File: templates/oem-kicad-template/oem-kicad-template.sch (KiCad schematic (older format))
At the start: 0 parts

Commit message: added icon to template, added atmega to template schematic
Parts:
- added IC?: ATMEGA16M1, Housings_QFP:TQFP-32_7x7mm_Pitch0.8mm, symbol ATMEGA16M1
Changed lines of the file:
@@
 LIBS:contrib
 LIBS:valves
+LIBS:formula
 EELAYER 25 0
 EELAYER END
@@
 Comment4 ""
 $EndDescr
+$Comp
+L ATMEGA16M1 IC?
+U 1 1 59E01442
+P 4950 4300
+F 0 "IC?" H 4000 6130 50  0000 L BNN
+F 1 "ATMEGA16M1" H 5450 2900 50  0000 L BNN
+F 2 "Housings_QFP:TQFP-32_7x7mm_Pitch0.8mm" H 4950 4300 50  0000 C CIN
+F 3 "" H 4950 4300 50  0000 C CNN
+	1    4950 4300
+	1    0    0    -1
+$EndComp
 $EndSCHEMATC

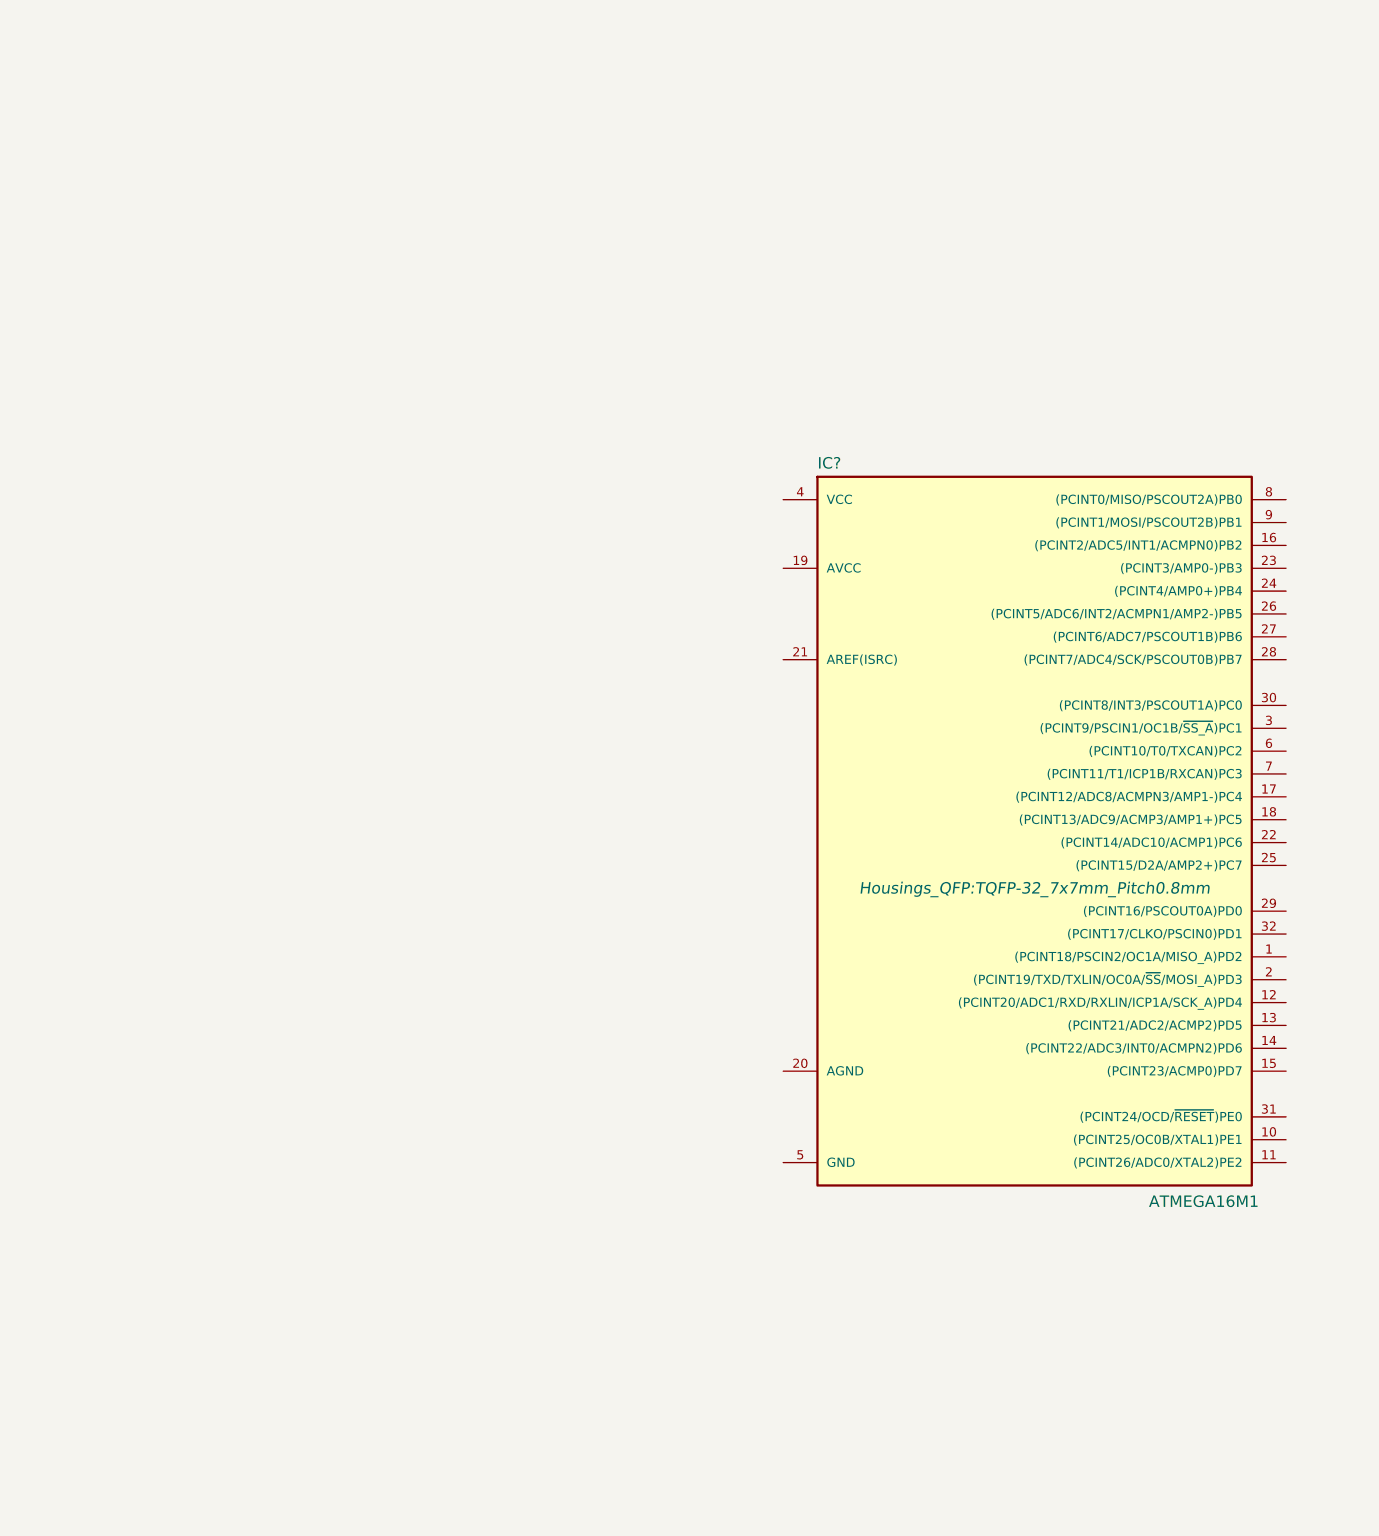
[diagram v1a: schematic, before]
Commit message: added buck to template, working on adding atmega
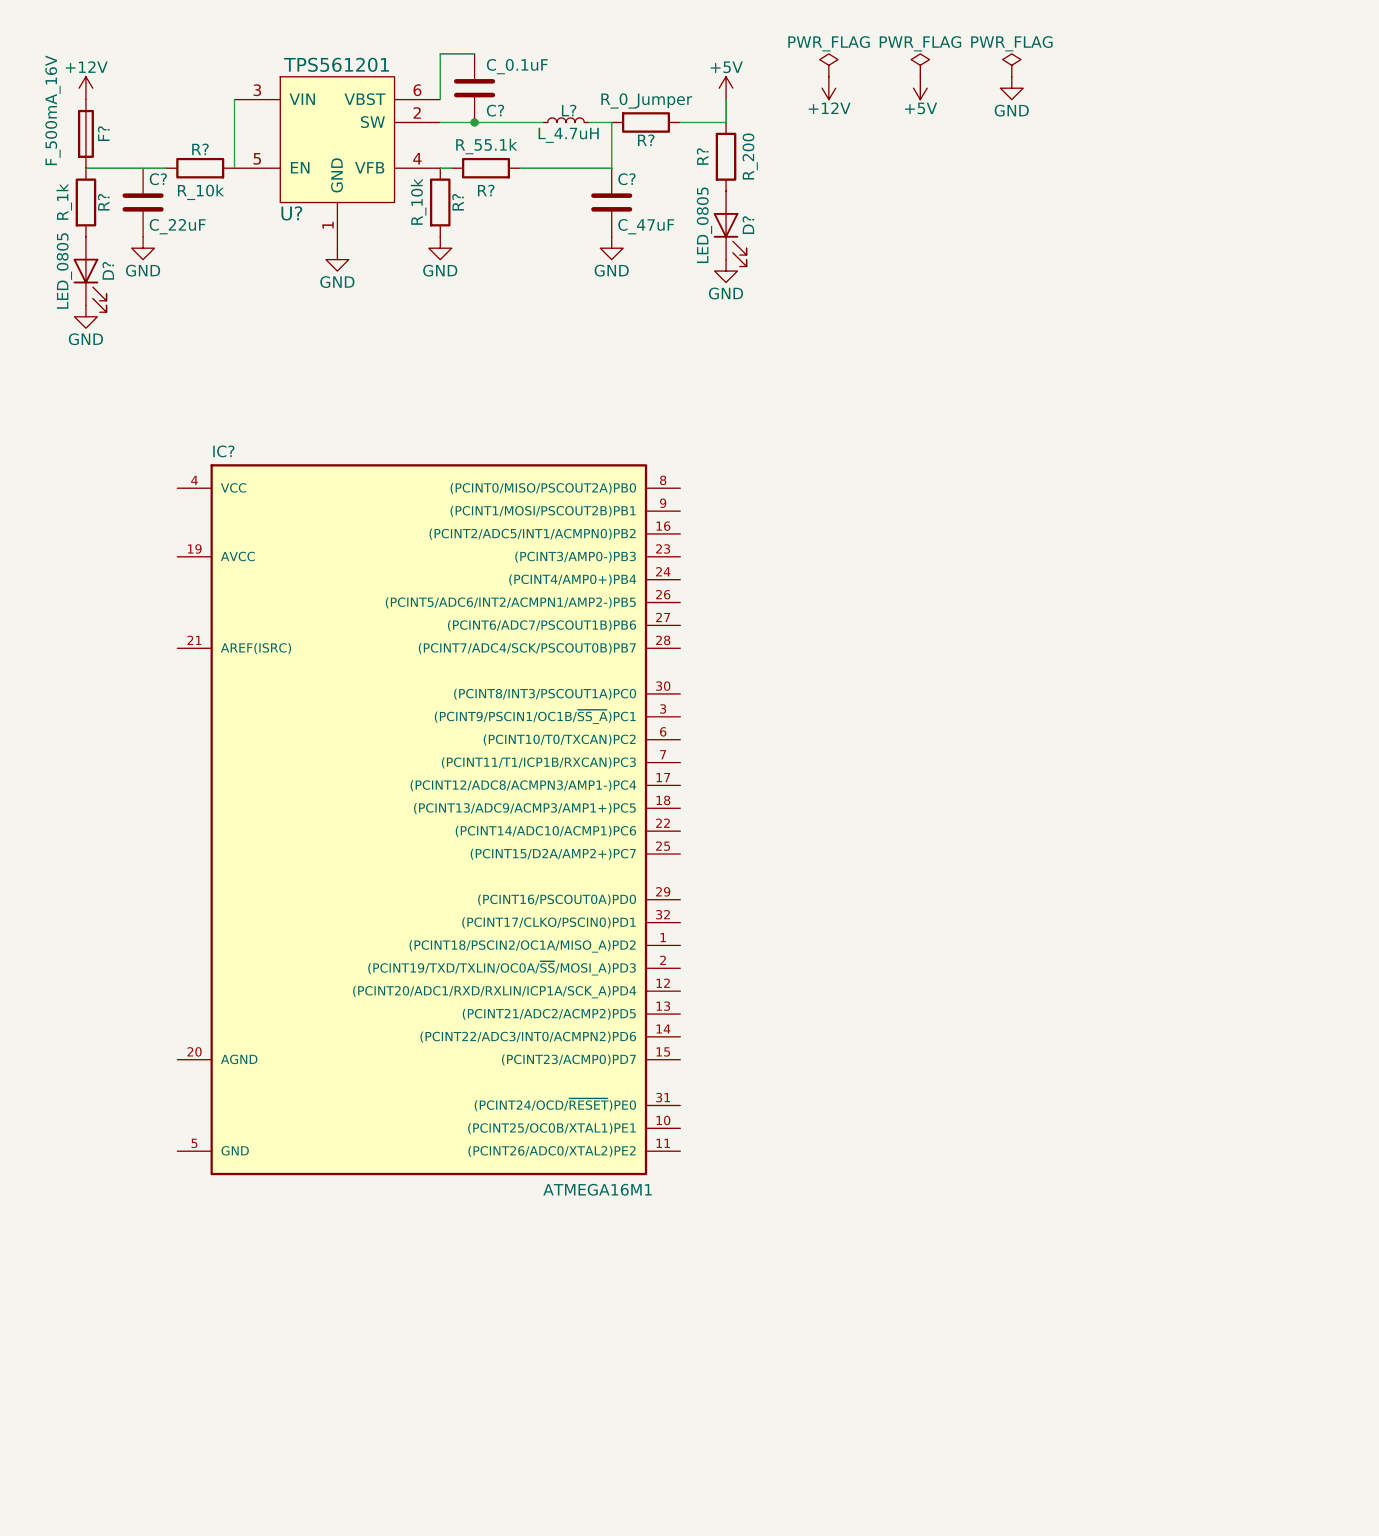
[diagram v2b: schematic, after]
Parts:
- removed IC?: ATMEGA16M1, Housings_QFP:TQFP-32_7x7mm_Pitch0.8mm, symbol ATMEGA16M1
- added C?: C_0.1uF, Capacitors_SMD:C_0805, symbol C_0.1uF
- added C?: C_22uF, Capacitors_SMD:C_1206, symbol C_22uF
- added C?: C_47uF, Capacitors_SMD:C_0805, symbol C_47uF
- added D? (x2): LED_0805, LEDs:LED_0805, symbol LED_0805
- added F?: F_500mA_16V, footprints:Fuse_1210, symbol F_500mA_16V
- added IC?: ATMEGA16M1, Housings_QFP:TQFP-32_7x7mm_Pitch0.8mm, symbol ATMEGA16M1
- added L?: L_4.7uH, footprints:4.7uH_Inductor_OEM, symbol L_4.7uH
- added R? (x2): R_10k, Resistors_SMD:R_0805, symbol R_10k
- added R?: R_1k, Resistors_SMD:R_0805, symbol R_1k
- added R?: R_55.1k, Resistors_SMD:R_0805, symbol R_55.1k
- added R?: R_200, Resistors_SMD:R_0805, symbol R_200
- added R?: R_0_Jumper, Resistors_SMD:R_2512, symbol R_0_Jumper
- added U?: TPS561201, TO_SOT_Packages_SMD:SOT-23-6, symbol TPS561201
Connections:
- new net: F?.2, R?.1, R?.1
- new net: R?.2, U?.3 (VIN), U?.5 (EN)
- new net: R?.1, R?.1, U?.4 (VFB)
- new net: D?.2 (A), R?.2 (x2)
- new net: C?.1, L?.2, R?.2, R?.2
- new net: C?.2, L?.1, U?.2 (SW)
- new net: C?.1, U?.6 (VBST)
- new net +12V: F?.1
- new net +5V: R?.1, R?.1
- new net GND: C?.2, C?.2, D?.1 (K), D?.1 (K), R?.2, U?.1 (GND)

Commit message: completed atmega schematic in template
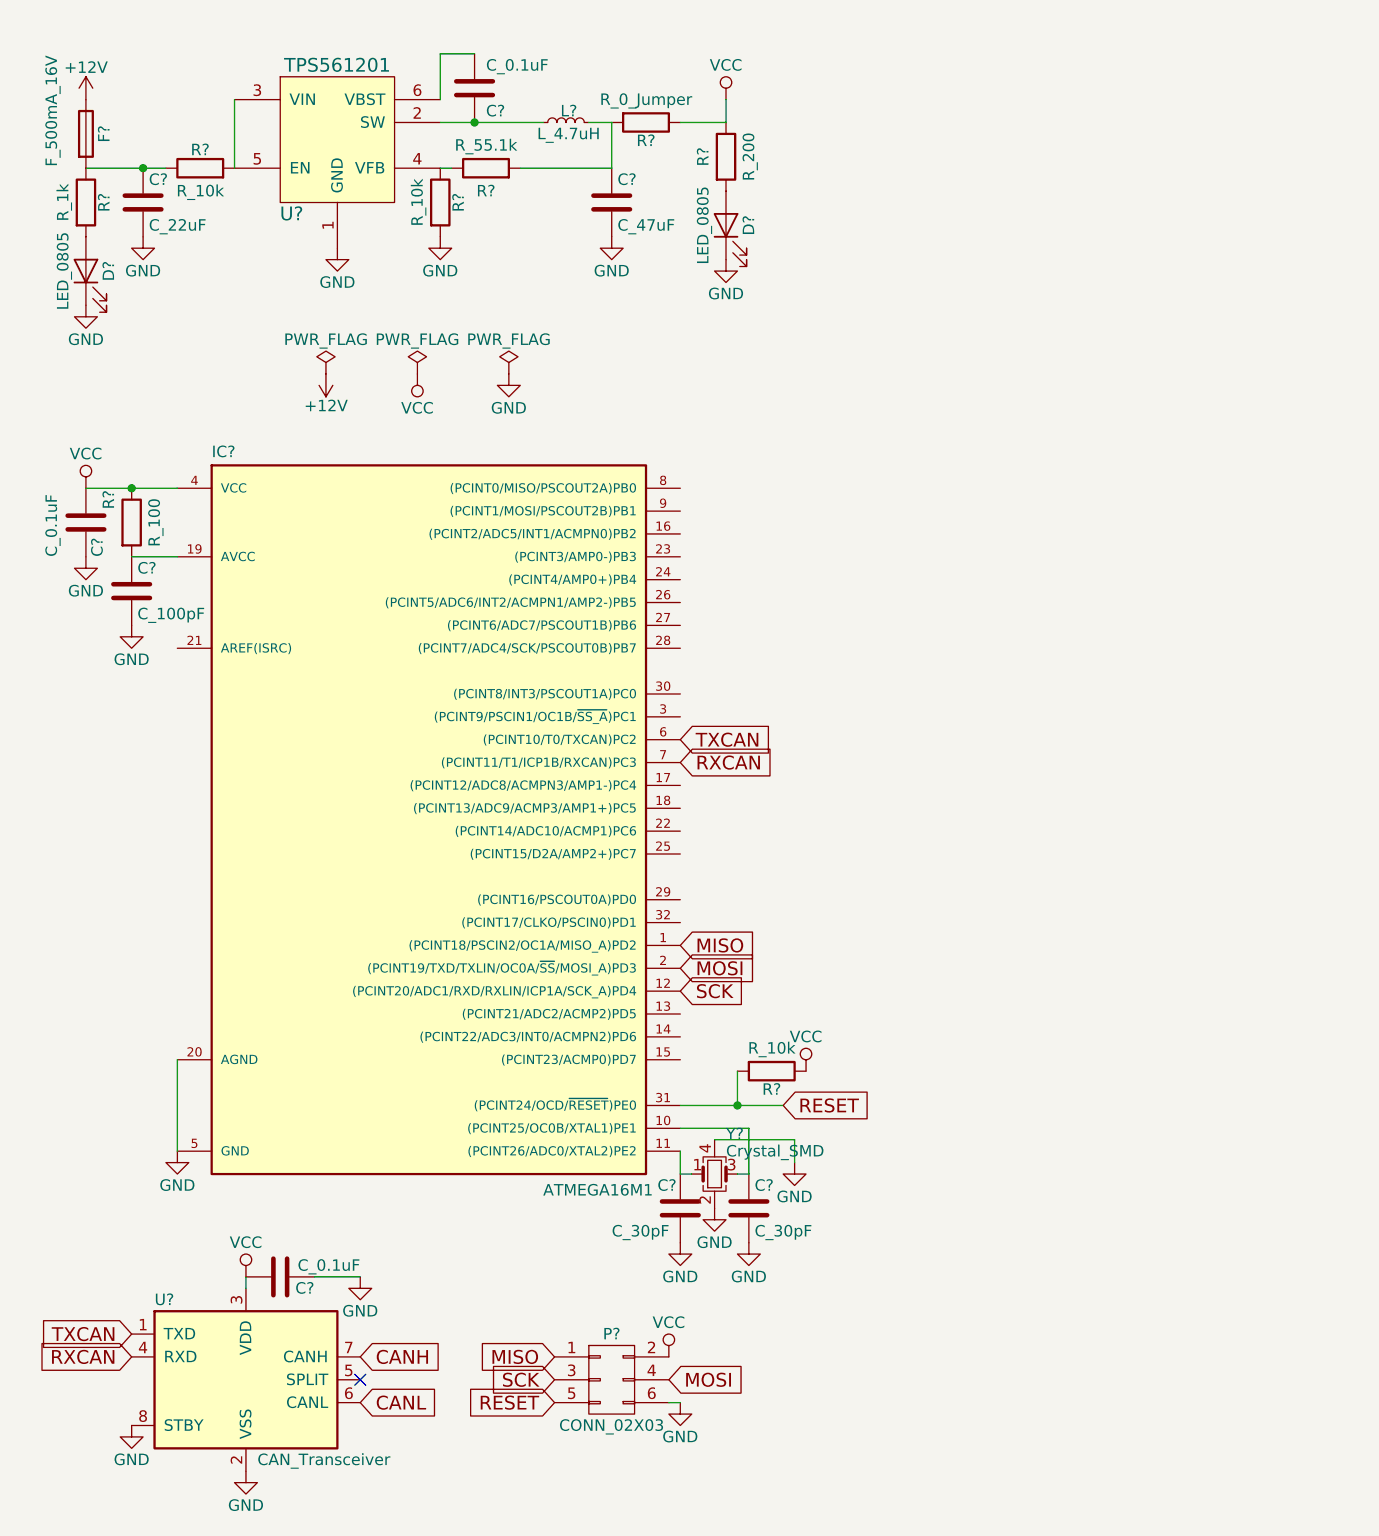
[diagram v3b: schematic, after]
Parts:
- removed IC?: ATMEGA16M1, Housings_QFP:TQFP-32_7x7mm_Pitch0.8mm, symbol ATMEGA16M1
- added C? (x2): C_0.1uF, Capacitors_SMD:C_0805, symbol C_0.1uF
- added C?: C_100pF, Capacitors_SMD:C_0805, symbol C_100pF
- added C? (x2): C_30pF, Capacitors_SMD:C_0805, symbol C_30pF
- added IC?: ATMEGA16M1, Housings_QFP:TQFP-32_7x7mm_Pitch0.8mm, symbol ATMEGA16M1
- added P?: CONN_02X03, footprints:Pin_Header_Straight_2x03, symbol CONN_02X03
- added R?: R_100, Resistors_SMD:R_0805, symbol R_100
- added R?: R_10k, Resistors_SMD:R_0805, symbol R_10k
- added U?: CAN_Transceiver, Housings_SOIC:SOIC-8_3.9x4.9mm_Pitch1.27mm, symbol CAN_Transceiver
- added Y?: Crystal_SMD, footprints:Crystal_SMD_FA238, symbol Crystal_SMD
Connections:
- net GND: now also C?.2, C?.2, C?.2, C?.2, C?.2, IC?.20 (AGND), IC?.5 (GND), P?.6 (P6), U?.2 (VSS), U?.8 (STBY), Y?.2, Y?.4
- net at F?.2, R?.1, R?.1: now also C?.1
- net +5V renamed VCC
- net VCC: now also C?.1, C?.1, IC?.4 (VCC), P?.2 (P2), R?.1, R?.1, U?.3 (VDD)
- new net: C?.1, IC?.19 (AVCC), R?.2
- new net: C?.1, IC?.10 ((PCINT25/OC0B/XTAL1)PE1), Y?.3
- new net: C?.1, IC?.11 ((PCINT26/ADC0/XTAL2)PE2), Y?.1
- new net CANH: U?.7 (CANH)
- new net CANL: U?.6 (CANL)
- new net MISO: IC?.1 ((PCINT18/PSCIN2/OC1A/MISO_A)PD2), P?.1 (P1)
- new net MOSI: IC?.2 ((PCINT19/TXD/TXLIN/OC0A/~SS~/MOSI_A)PD3), P?.4 (P4)
- new net RESET: IC?.31 ((PCINT24/OCD/~RESET~)PE0), P?.5 (P5), R?.2
- new net RXCAN: IC?.7 ((PCINT11/T1/ICP1B/RXCAN)PC3), U?.4 (RXD)
- new net SCK: IC?.12 ((PCINT20/ADC1/RXD/RXLIN/ICP1A/SCK_A)PD4), P?.3 (P3)
- new net TXCAN: IC?.6 ((PCINT10/T0/TXCAN)PC2), U?.1 (TXD)
- no-connect marks 0 -> 1
